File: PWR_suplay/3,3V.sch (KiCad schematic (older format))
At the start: 3 parts, among them U2 APE8865N-33-HF-3

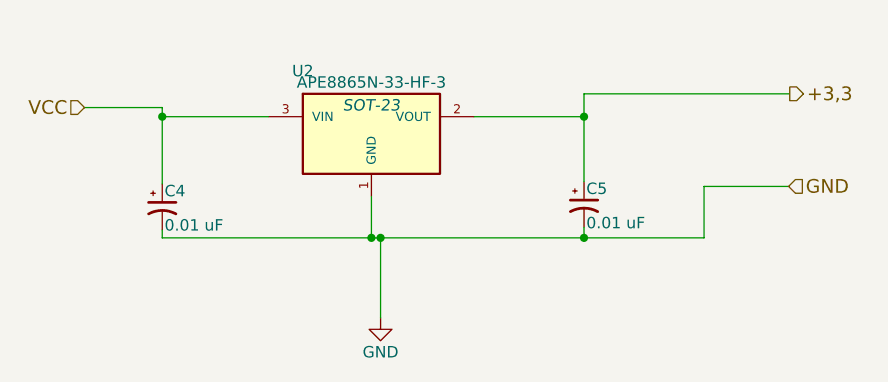
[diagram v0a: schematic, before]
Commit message: izlaboju kludu PWR un papildijnaju battery holder ar kontuuram
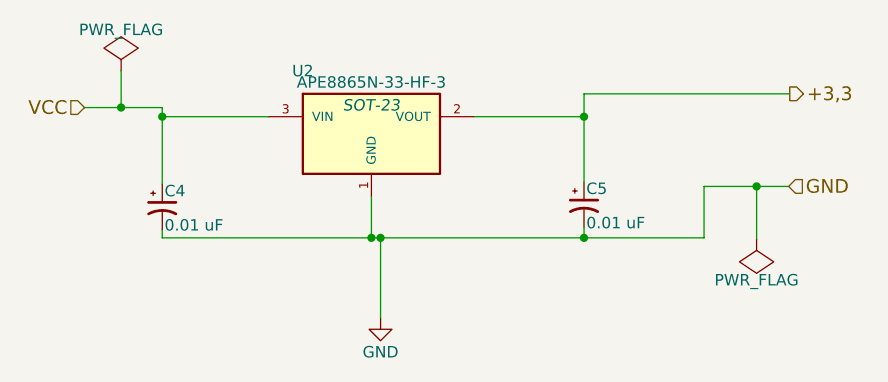
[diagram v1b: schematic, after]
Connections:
- wire segments 14 -> 16
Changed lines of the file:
@@
 	1    0    0    -1
 $EndComp
+$Comp
+L PWR_FLAG #FLG03
+U 1 1 5910B761
+P 4405 3245
+F 0 "#FLG03" H 4405 3340 50  0001 C CNN
+F 1 "PWR_FLAG" H 4405 3425 50  0000 C CNN
+F 2 "" H 4405 3245 50  0000 C CNN
+F 3 "" H 4405 3245 50  0000 C CNN
+	1    4405 3245
+	1    0    0    -1
+$EndComp
+$Comp
+L PWR_FLAG #FLG04
+U 1 1 5910B7DF
+P 7185 3980
+F 0 "#FLG04" H 7185 4075 50  0001 C CNN
+F 1 "PWR_FLAG" H 7185 4160 50  0000 C CNN
+F 2 "" H 7185 3980 50  0000 C CNN
+F 3 "" H 7185 3980 50  0000 C CNN
+	1    7185 3980
+	-1   0    0    1
+$EndComp
+Wire Wire Line
+	4405 3245 4405 3405
+Connection ~ 4405 3405
+Wire Wire Line
+	7185 3980 7185 3750
+Connection ~ 7185 3750
 $EndSCHEMATC

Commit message: izlaboju teiktas kluas, tagad vajadzetu but
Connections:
- wire segments 16 -> 15
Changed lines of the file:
@@
 L GND #PWR02
 U 1 1 590F5689
-P 5540 4325
-F 0 "#PWR02" H 5540 4075 50  0001 C CNN
-F 1 "GND" H 5540 4175 50  0000 C CNN
-F 2 "" H 5540 4325 50  0000 C CNN
-F 3 "" H 5540 4325 50  0000 C CNN
-	1    5540 4325
+P 5500 4325
+F 0 "#PWR02" H 5500 4075 50  0001 C CNN
+F 1 "GND" H 5500 4175 50  0000 C CNN
+F 2 "" H 5500 4325 50  0000 C CNN
+F 3 "" H 5500 4325 50  0000 C CNN
+	1    5500 4325
 	1    0    0    -1
 $EndComp
@@
 	6430 3975 6430 3930
 Wire Wire Line
-	5540 3975 5540 4325
-Wire Wire Line
 	6430 3345 6430 3730
 Wire Wire Line
@@
 Connection ~ 6430 3445
 Connection ~ 4585 3445
-Connection ~ 5540 3975
 Wire Wire Line
 	6430 3445 6430 3440
 Connection ~ 5500 3975
 Wire Wire Line
-	5500 3795 5500 3975
+	5500 3795 5500 4325
 Wire Wire Line
 	5050 3445 4585 3445
